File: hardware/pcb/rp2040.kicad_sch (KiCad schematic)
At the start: 37 parts, among them SW101 BOOTSEL, SW102 CM0 BOOT, U101 RP2040, U102 W25Q128JVSIQ, Y101 12MHz

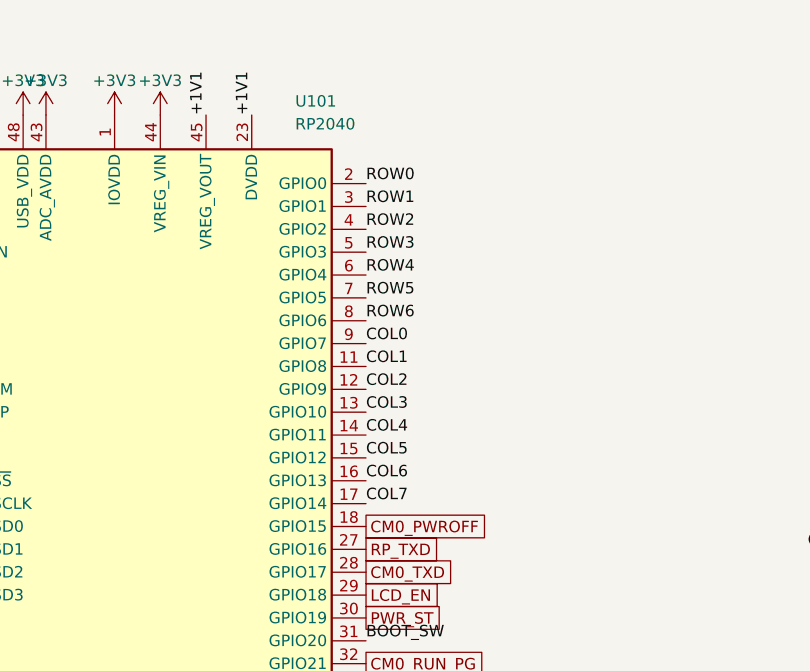
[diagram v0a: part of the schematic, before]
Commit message: Add 42-key matrix sheet, layout, and USB-C part
- Key layout from Smidr (KLE format, 42 keys) in hardware/layout,
  with the 7x6 COL2ROW matrix mapping proven on the blad keyboard
- Keymatrix sheet: 42 Choc hotswap switches and 1N4148W diodes
  (C81598, Basic), every pin labeled; RP2040 ROW/COL nets are now
  global labels, GPIO13/14 freed as spares
- USB-C receptacles J1/J2 set to HRO TYPE-C-31-M-12 (C165948)
- Power sheet: CC lines reach the RP2040 ADC again
- Docs: design decisions, pin assignment, keymatrix spec and
  reference, open items

Full project netlist matches all 141 intended nets; ERC has no errors.

Co-Authored-By: Claude Opus 5.5 <noreply@anthropic.com>
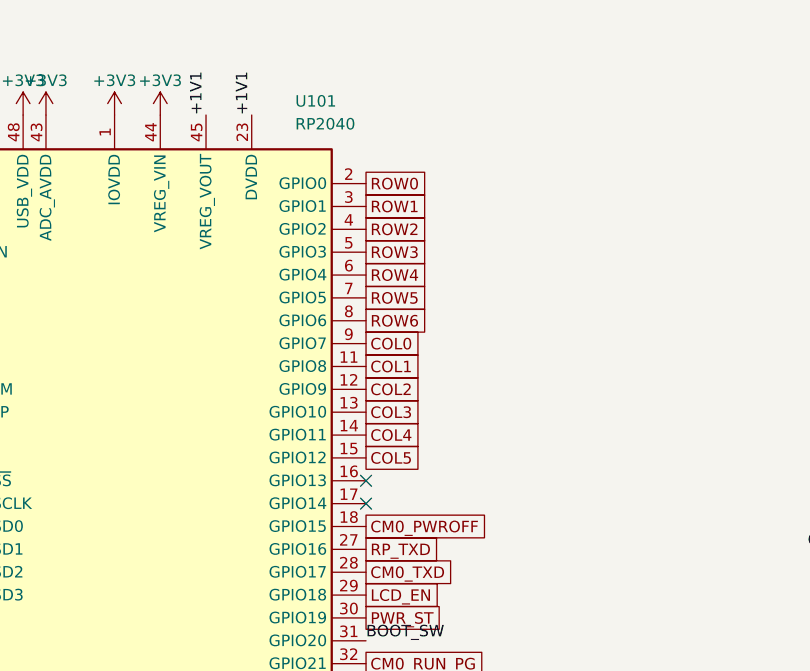
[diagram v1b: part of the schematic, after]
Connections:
- net COL6: no longer names the net of U101.16 (GPIO13)
- net COL7: no longer names the net of U101.17 (GPIO14)
- no-connect marks 0 -> 2

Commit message: Assign 0603 parts, use 30k for ILM, and switch the LDO to AP2127
Give every resistor and capacitor a 0603 footprint and an LCSC number
(Basic where possible), change the ILM resistor to a 30k Basic part,
and replace the XC6206 with an AP2127N-3.3 from stock. Record the
decisions and drop the resolved open items.

Co-Authored-By: Claude Opus 5.5 <noreply@anthropic.com>
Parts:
- C101, C102, C103, C104, C105, C106, C107, C108, C111, C112, C115: footprint (none) -> Capacitor_SMD:C_0603_1608Metric; LCSC (none) -> C14663
- C109, C110: footprint (none) -> Capacitor_SMD:C_0603_1608Metric; LCSC (none) -> C15849
- C113, C114: footprint (none) -> Capacitor_SMD:C_0603_1608Metric; LCSC (none) -> C1663
- R101, R102, R107, R108, R109, R110: footprint (none) -> Resistor_SMD:R_0603_1608Metric; LCSC (none) -> C21190
- R103, R104: footprint (none) -> Resistor_SMD:R_0603_1608Metric; LCSC (none) -> C25804
- R105, R106: footprint (none) -> Resistor_SMD:R_0603_1608Metric; LCSC (none) -> C25190

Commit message: Add audio, microSD and keyboard I2C, and place parts on the PCB
Schematics:
- Swap the MAX98357A for the TLV320DAC3100 (headphone and speaker out).
  A 12 MHz oscillator drives MCLK and the codec is the I2S clock master,
  so the stock simple-audio-card works without a custom machine driver.
- Add the microSD slot for the CM0Lite; the SD pull-ups are footprints only.
- Add HID over I2C from the RP2040 to the CM0 (KB_SDA/KB_SCL/KB_INT) on
  i2c-gpio, so the keyboard works on stock Raspberry Pi OS. Add test pads.
- Use power symbols for +1V1, assign footprints and LCSC numbers, and
  fix global label shapes.

PCB: 228.6 x 146.2 mm outline and a provisional bottom-side placement,
with HID USB top-left and Linux USB top-right. Add footprints for the CM0,
TPS2121 (RUX), the 22-pin DSI FPC and the CR2032 holder.

Docs: record the decisions and open items. Add a draft device tree
overlay for the audio codec.

Co-Authored-By: Claude Opus 5.5 <noreply@anthropic.com>
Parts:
- added TP108: KB_INT, TestPoint:TestPoint_Pad_D1.5mm, symbol Connector:TestPoint
- C113, C114: value 33p -> 27p; LCSC C1663 -> C107045
- SW101, SW102: footprint (none) -> Button_Switch_SMD:SW_Push_1P1T_XKB_TS-1187A; LCSC (none) -> C318884
- TP101, TP102, TP103, TP104, TP105, TP106, TP107: footprint (none) -> TestPoint:TestPoint_Pad_D1.5mm
- U102: value W25Q128JVSIQ -> W25Q128JVPIQ; footprint Package_SO:SOIC-8_5.3x5.3mm_P1.27mm -> Package_SON:WSON-8-1EP_6x5mm_P1.27mm_EP3.4x4.3mm; LCSC C97521 -> C190862
- Y101: footprint (none) -> Crystal:Crystal_SMD_3225-4Pin_3.2x2.5mm; LCSC C9002 -> C521581; MPN (none) -> XXHBBCNANF-12.000000MHZ
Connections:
- net KB_INT: now reaches U101.16 (GPIO13)
- net KB_INT: now also TP108.1
- net BOOTSEL_R: no longer names the net of R102.1, SW101.2
- net CC_ADC0: no longer names the net of R107.2, U101.38 (GPIO26/ADC0)
- net CC_ADC1: no longer names the net of R108.2, U101.39 (GPIO27/ADC1)
- net CC_ADC2: no longer names the net of R109.2, U101.40 (GPIO28/ADC2)
- net CC_ADC3: no longer names the net of R110.2, U101.41 (GPIO29/ADC3)
- net GPIO24 renamed KB_SDA
- net GPIO25 renamed KB_SCL
- net QSPI_SS renamed ~{QSPI_SS}
- net USB_DM_MCU: no longer names the net of R106.1, U101.46 (USB_DM)
- net USB_DP_MCU: no longer names the net of R105.1, U101.47 (USB_DP)
- net XIN: no longer names the net of C113.1, U101.20 (XIN), Y101.1
- net XOUT: no longer names the net of R101.1
- net XOUT: now also C114.1, Y101.3; no longer U101.21 (XOUT)
- removed net XTAL_OUT: C114.1, R101.2, Y101.3
- new net: R101.2, U101.21 (XOUT)
- no-connect marks 2 -> 1
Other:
- note removed: "1.1V（DVDD）"
- note removed: "CC → ADC"
- note removed: "USB（Port A）"
- note removed: "シート外へ"
- note removed: "水晶 12 MHz"
- note removed: "電源のパスコン（IOVDD ×6、USB_VDD、ADC_AVDD、VREG）"
- moved on the sheet: C101, C102, C103, C104, C105, C106, C107, C108, C109, C110, C111, C112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

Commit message: Add per-key RGB, finish schematic wiring, and document HID over I2C
- Add SK6812MINI-E per-key RGB with a switched +5V_LED rail and an
  AHCT buffer on the data line; remove SW102 to free GPIO20
- Use D_Small for the matrix diodes and replace labels with wires
- Tidy the keymatrix sheet layout without changing connectivity
- Document the HID over I2C keyboard path, back-power rules and
  role split across README and docs

Co-Authored-By: Claude Opus 5.5 <noreply@anthropic.com>
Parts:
- removed R104: 10k, Resistor_SMD:R_0603_1608Metric, symbol Device:R
- removed SW102: CM0 BOOT, Button_Switch_SMD:SW_Push_1P1T_XKB_TS-1187A, symbol Switch:SW_Push
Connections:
- net RGB_DATA: now reaches U101.17 (GPIO14)
- net BOOT_SW renamed RGB_EN
- no-connect marks 1 -> 0
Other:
- note removed: "CM0 の USB ブート要求"
- moved on the sheet: R107, R108, R109, R110
